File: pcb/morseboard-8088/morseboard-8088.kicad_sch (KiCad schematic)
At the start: 33 parts, among them J1 USB_B, SW1 SW_SPDT, SW3 RES, SW4 NMI, U1 8088, U2 74HCT573, U3 74HCT573, U4 74HCT245, U5 SST39SF040, U7 74HCT02, U8 74HCT00, U9 AS6C4008-55PCN, X1 TCXO-14

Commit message: Initial commit TL16C550
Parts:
- added U10: 74HCT273, Package_DIP:DIP-20_W7.62mm_Socket, symbol 74xx:74HC273
- added U11: ~, symbol tl16c550:TL16C550C-FN
- added U6: 74HCT138, Package_DIP:DIP-16_W7.62mm_Socket, symbol 74xx:74HC138
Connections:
- net A0: now also U11.31 (A0)
- net A1: now also U11.30 (A1)
- net A2: now also U11.29 (A2)
- net A5: now also U6.1 (A0)
- net A6: now also U6.2 (A1)
- net A7: now also U6.3 (A2)
- net D0: now also U10.3 (D0), U11.2 (D0)
- net D1: now also U10.4 (D1), U11.3 (D1)
- net D2: now also U10.7 (D2), U11.4 (D2)
- net D3: now also U10.8 (D3), U11.5 (D3)
- net D4: now also U10.13 (D4), U11.6 (D4)
- net D5: now also U10.14 (D5), U11.7 (D5)
- net D6: now also U10.17 (D6), U11.8 (D6)
- net D7: now also U10.18 (D7), U11.9 (D7)
- net GND: now also U10.10 (GND), U11.21 (WR2), U11.22 (GND), U11.25 (RD2), U11.28 (~{ADS}), U6.4 (~{E0}), U6.5 (~{E1}), U6.8 (GND); no longer U1.18 (INTR)
- net LATCH: now also U10.11 (Cp)
- net RES: now also U11.39 (MR)
- net VCC: now also U10.20 (VCC), U11.14 (CS0), U11.15 (CS1), U11.44 (VCC), U6.16 (VCC)
- net ~{IO00}: now also U6.15 (~{Y0})
- net ~{M}: now also U6.6 (E2)
- net ~{RD}: now also U11.24 (~{RD1})
- net ~{RES}: now also U10.1 (~{Mr})
- net ~{WR}: now also U11.20 (~{WR1})
- net ~{INTA}: now reaches U1.24 (~{INTA})
- new net INTR: U1.18 (INTR), U11.33 (INTRPT)
- new net L0: U10.2 (Q0)
- new net L1: U10.5 (Q1)
- new net L2: U10.6 (Q2)
- new net L3: U10.9 (Q3)
- new net L4: U10.12 (Q4)
- new net L5: U10.15 (Q5)
- new net L6: U10.16 (Q6)
- new net L7: U10.19 (Q7)
- new net RxD: U11.11 (SIN)
- new net TxD: U11.13 (SOUT)
- new net ~{IO01}: U11.16 (~{CS2}), U6.14 (~{Y1})
- no-connect marks 12 -> 20
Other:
- removed sheet output

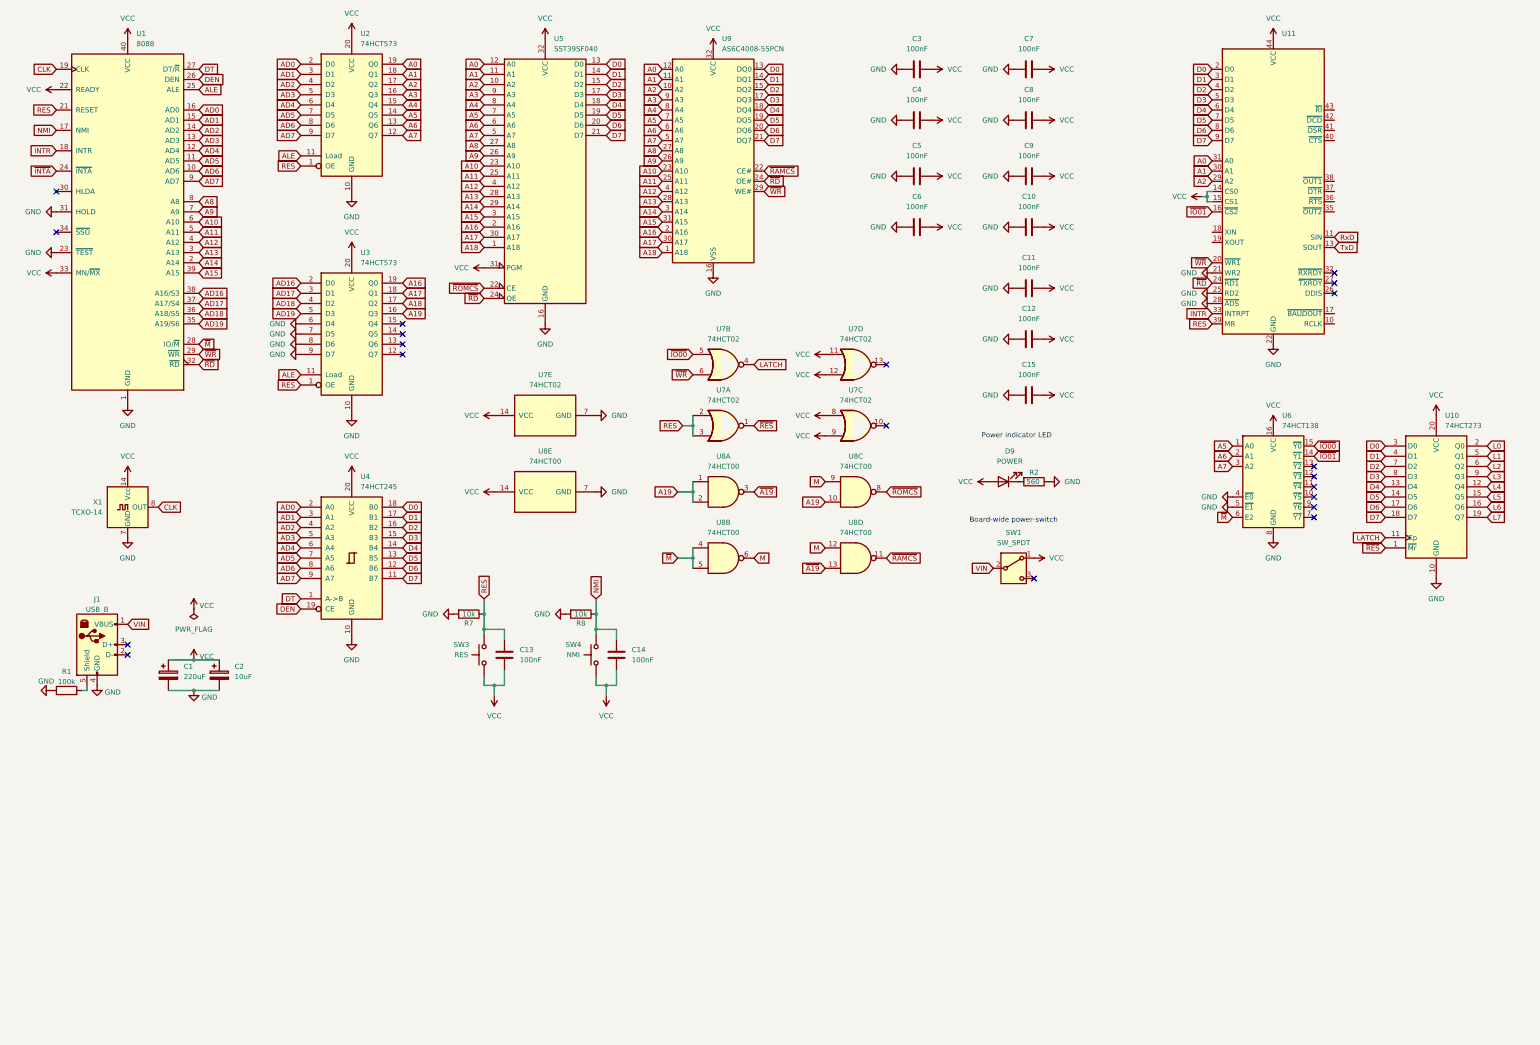
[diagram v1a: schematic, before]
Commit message: Further revising second 8088 SBC prototype
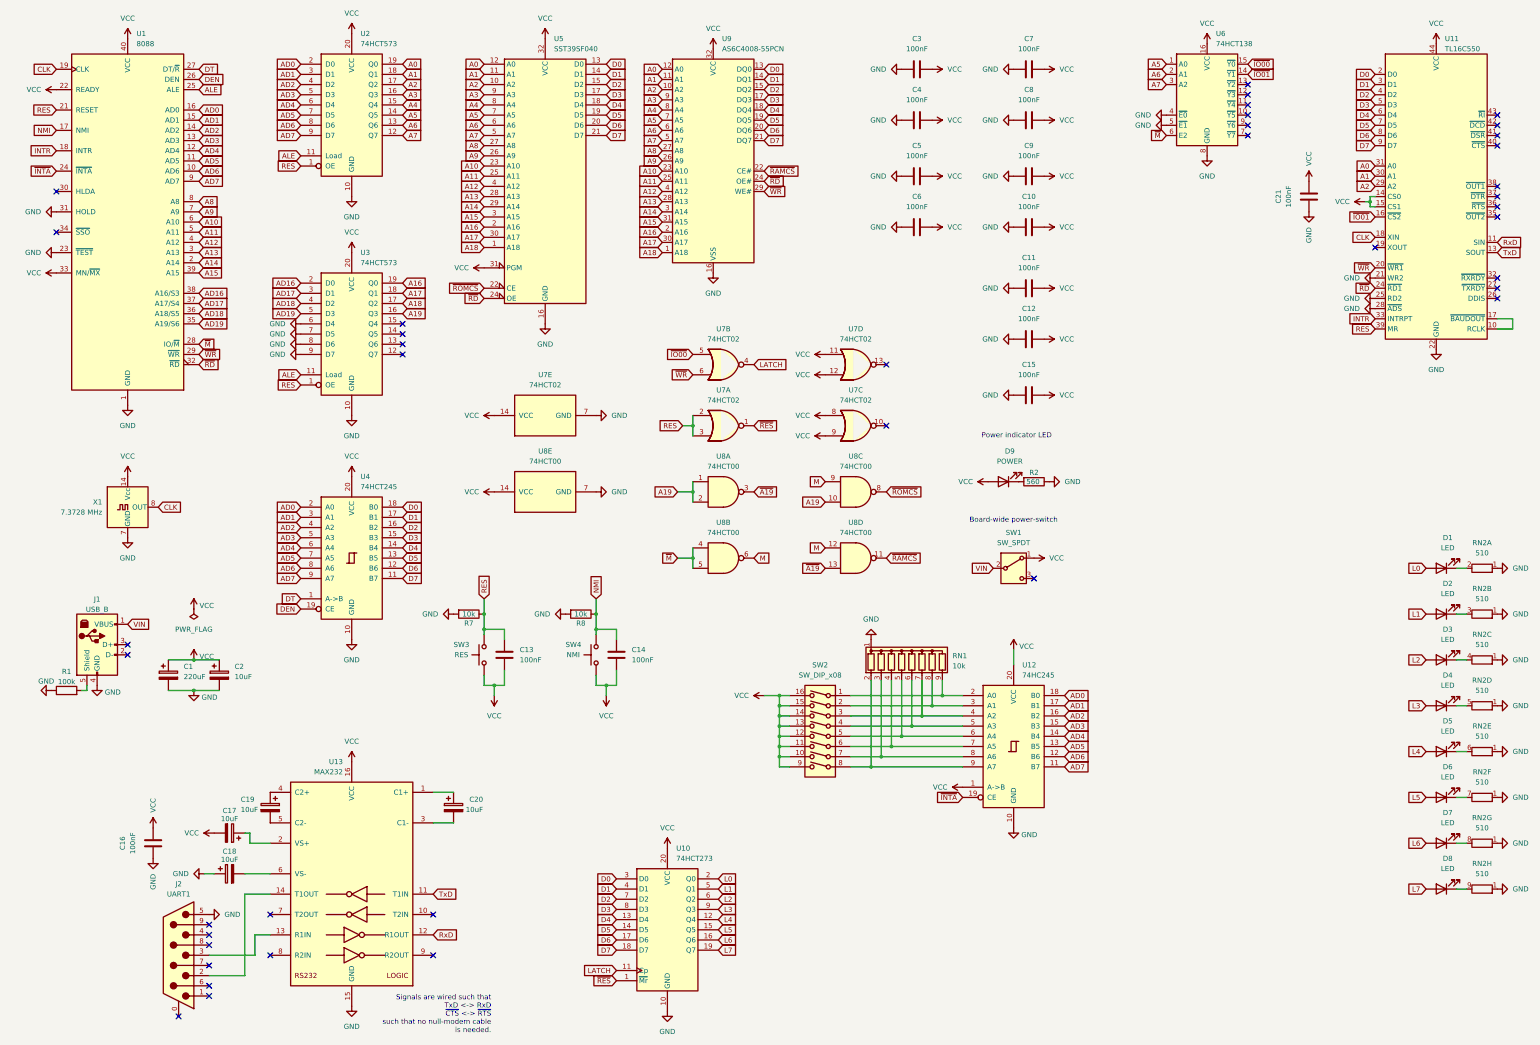
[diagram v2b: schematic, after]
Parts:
- added C16, C21: 100nF, Capacitor_THT:C_Disc_D5.0mm_W2.5mm_P5.00mm, symbol Device:C
- added C17, C18, C19, C20: 10uF, Capacitor_THT:CP_Radial_D5.0mm_P2.50mm, symbol Device:C_Polarized
- added D1, D2, D3, D4, D5, D6, D7, D8: LED, LED_THT:LED_D5.0mm, symbol Device:LED
- added J2: UART1, Connector_Dsub:DSUB-9_Pins_Horizontal_P2.77x2.84mm_EdgePinOffset4.94mm_Housed_MountingHolesOffset4.94mm, symbol Connector:DE9_Pins_MountingHoles
- added RN1: 10k, Resistor_THT:R_Array_SIP9, symbol Device:R_Network08
- added RN2: 510, Resistor_THT:R_Array_SIP9, symbol Device:R_Network08_Split
- added SW2: SW_DIP_x08, Button_Switch_THT:SW_DIP_SPSTx08_Slide_9.78x22.5mm_W7.62mm_P2.54mm, symbol Switch:SW_DIP_x08
- added U12: 74HC245, Package_DIP:DIP-20_W7.62mm_Socket, symbol 74xx:74HC245
- added U13: MAX232, Package_DIP:DIP-16_W7.62mm_Socket, symbol Interface_UART:MAX232
- U11: value ~ -> TL16C550; footprint (none) -> Package_LCC:PLCC-44_THT-Socket
- X1: value TCXO-14 -> 7.3728 MHz
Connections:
- net AD0: now also U12.18 (B0)
- net AD1: now also U12.17 (B1)
- net AD2: now also U12.16 (B2)
- net AD3: now also U12.15 (B3)
- net AD4: now also U12.14 (B4)
- net AD5: now also U12.13 (B5)
- net AD6: now also U12.12 (B6)
- net AD7: now also U12.11 (B7)
- net CLK: now also U11.18 (XIN)
- net GND: now also C16.2, C18.1, C21.2, J2.5, RN1.1 (common), RN2.1 (R1), RN2.1 (R1), RN2.1 (R1), RN2.1 (R1), RN2.1 (R1), RN2.1 (R1), RN2.1 (R1), RN2.1 (R1), U12.10 (GND), U13.15 (GND)
- net L0: now also D1.2 (A)
- net L1: now also D2.2 (A)
- net L2: now also D3.2 (A)
- net L3: now also D4.2 (A)
- net L4: now also D5.2 (A)
- net L5: now also D6.2 (A)
- net L6: now also D7.2 (A)
- net L7: now also D8.2 (A)
- net RxD: now also U13.12 (R1OUT)
- net TxD: now also U13.11 (T1IN)
- net VCC: now also C16.1, C17.2, C21.1, SW2.10, SW2.11, SW2.12, SW2.13, SW2.14, SW2.15, SW2.16, SW2.9, U12.1 (A->B), U12.20 (VCC), U13.16 (VCC)
- net ~{INTA}: now also U12.19 (CE)
- net at U11.10 (RCLK): now also U11.17 (~{BAUDOUT})
- new net: D5.1 (K), RN2.6 (R5.2)
- new net: D6.1 (K), RN2.7 (R6.2)
- new net: C17.1, U13.2 (VS+)
- new net: C18.2, U13.6 (VS-)
- new net: D3.1 (K), RN2.4 (R3.2)
- new net: D8.1 (K), RN2.9 (R8.2)
- new net: D2.1 (K), RN2.3 (R2.2)
- new net: J2.2, U13.14 (T1OUT)
- new net: J2.3, U13.13 (R1IN)
- new net: RN1.9 (R8), SW2.1, U12.2 (A0)
- new net: RN1.8 (R7), SW2.2, U12.3 (A1)
- new net: RN1.7 (R6), SW2.3, U12.4 (A2)
- new net: RN1.6 (R5), SW2.4, U12.5 (A3)
- new net: RN1.5 (R4), SW2.5, U12.6 (A4)
- new net: RN1.4 (R3), SW2.6, U12.7 (A5)
- new net: RN1.3 (R2), SW2.7, U12.8 (A6)
- new net: RN1.2 (R1), SW2.8, U12.9 (A7)
- new net: C20.1, U13.1 (C1+)
- new net: C20.2, U13.3 (C1-)
- new net: C19.1, U13.4 (C2+)
- new net: C19.2, U13.5 (C2-)
- new net: D1.1 (K), RN2.2 (R1.2)
- new net: D7.1 (K), RN2.8 (R7.2)
- new net: D4.1 (K), RN2.5 (R4.2)
- no-connect marks 20 -> 40
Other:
- note added: "Signals are wired such that TxD <-> RxD ~{CTS} <-> ~{RTS} such that no null-modem cable is needed."
- moved on the sheet: U10, U11, U6

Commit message: Updating schematic and board
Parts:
- added H1, H2, H3, H4: MountingHole, MountingHole:MountingHole_3.2mm_M3_DIN965, symbol Mechanical:MountingHole
- added J3: TxD, Connector_PinHeader_2.54mm:PinHeader_1x03_P2.54mm_Vertical, symbol Connector:Conn_01x03_Pin
- added J4: ~{CTS}, Connector_PinHeader_2.54mm:PinHeader_1x03_P2.54mm_Vertical, symbol Connector:Conn_01x03_Pin
- added J5: RxD, Connector_PinHeader_2.54mm:PinHeader_1x03_P2.54mm_Vertical, symbol Connector:Conn_01x03_Pin
- added J6: ~{RTS}, Connector_PinHeader_2.54mm:PinHeader_1x03_P2.54mm_Vertical, symbol Connector:Conn_01x03_Pin
- SW2: value SW_DIP_x08 -> INTPORT
- U1: footprint Package_DIP:DIP-40_W15.24mm -> Package_DIP:DIP-40_W15.24mm_Socket
- U9: footprint Package_DIP:DIP-32_W15.24mm -> Package_DIP:DIP-32_W15.24mm_Socket
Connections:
- net ~{RTS}: now reaches U11.36 (~{RTS})
- net ~{RTS}: now also U13.9 (R2OUT)
- net ~{CTS}: now reaches U11.40 (~{CTS})
- net ~{CTS}: now also U13.10 (T2IN)
- net T1OUT: now reaches U13.14 (T1OUT)
- net T1OUT: now also J3.2 (Pin_2); no longer J2.2
- net R1IN: now reaches U13.13 (R1IN)
- net R1IN: now also J5.2 (Pin_2); no longer J2.3
- net UART7: now reaches J2.7
- net UART7: now also J4.1 (Pin_1), J6.1 (Pin_1)
- net UART8: now reaches J2.8
- net UART8: now also J4.3 (Pin_3), J6.3 (Pin_3)
- net T2OUT: now reaches U13.7 (T2OUT)
- net T2OUT: now also J4.2 (Pin_2)
- net R2IN: now reaches U13.8 (R2IN)
- net R2IN: now also J6.2 (Pin_2)
- new net UART2: J2.2, J3.1 (Pin_1), J5.1 (Pin_1)
- new net UART3: J2.3, J3.3 (Pin_3), J5.3 (Pin_3)
- no-connect marks 40 -> 31
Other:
- moved on the sheet: C16, C17, C18, C19, C20, J2, U13

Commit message: Prerouting commit
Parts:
- removed C13: 100nF, Capacitor_THT:C_Disc_D5.0mm_W2.5mm_P5.00mm, symbol Device:C
- removed R7: 10k, Resistor_THT:R_Axial_DIN0207_L6.3mm_D2.5mm_P7.62mm_Horizontal, symbol Device:R
- removed SW3: RES, Button_Switch_THT:SW_PUSH_6mm, symbol Switch:SW_Push
- added SW6: RESET, Button_Switch_THT:SW_PUSH_6mm, symbol Switch:SW_Push
- added U14: DS1813, Package_TO_SOT_THT:TO-92, symbol Connector:Conn_01x03_Pin
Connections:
- net GND: now also SW6.1, U14.3 (Pin_3)
- net RES: now also U7.1; no longer U7.2, U7.3
- net VCC: now also U14.2 (Pin_2)
- net ~{CTS}: now also U13.9 (R2OUT); no longer U13.10 (T2IN)
- net ~{RES}: now also U7.2, U7.3, SW6.2, U14.1 (Pin_1); no longer U7.1
- net ~{RTS}: now also U13.10 (T2IN); no longer U13.9 (R2OUT)
- no-connect marks 31 -> 32
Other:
- note added: "0x00"
- note added: "0x20"

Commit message: Protoype #1 of SBC
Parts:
- added C13: 100nF, Capacitor_THT:C_Disc_D5.0mm_W2.5mm_P5.00mm, symbol Device:C
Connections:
- net GND: now also C13.2
- net VCC: now also C13.1
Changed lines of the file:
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@@
 	)
 	(symbol
+		(lib_id "power:VCC")
+		(at 299.72 113.03 270)
+		(unit 1)
+		(exclude_from_sim no)
+		(in_bom yes)
+		(on_board yes)
+		(dnp no)
+		(fields_autoplaced yes)
+		(property "Reference" "#PWR076"
+			(at 295.91 113.03 0)
+			(effects
+				(font
+					(size 1.27 1.27)
+				)
+				(hide yes)
+			)
+		)
+		(property "Value" "VCC"
+			(at 303.53 113.0299 90)
+			(effects
+				(font
+					(size 1.27 1.27)
+				)
+				(justify left)
+			)
+		)
+		(property "Footprint" ""
+			(at 299.72 113.03 0)
+			(effects
+				(font
+					(size 1.27 1.27)
+				)
+				(hide yes)
+			)
+		)
+		(property "Datasheet" ""
+			(at 299.72 113.03 0)
+			(effects
+				(font
+					(size 1.27 1.27)
+				)
+				(hide yes)
+			)
+		)
+		(property "Description" "Power symbol creates a global label with name \"VCC\""
+			(at 299.72 113.03 0)
+			(effects
+				(font
+					(size 1.27 1.27)
+				)
+				(hide yes)
+			)
+		)
+		(pin "1"
+		)
+		(instances
+			(project "morseboard-8088"
+				(path "/27cb38f9-12de-466e-a080-2dfa091752ed"
+					(reference "#PWR076")
+					(unit 1)
+				)
+			)
+		)
+	)
+	(symbol
 		(lib_id "power:GND")
 		(at 43.18 148.59 0)
@@
 	(symbol
 		(lib_id "power:GND")
+		(at 292.1 113.03 270)
+		(unit 1)
+		(exclude_from_sim no)
+		(in_bom yes)
+		(on_board yes)
+		(dnp no)
+		(fields_autoplaced yes)
+		(property "Reference" "#PWR075"
+			(at 285.75 113.03 0)
+			(effects
+				(font
+					(size 1.27 1.27)
+				)
+				(hide yes)
+			)
+		)
+		(property "Value" "GND"
+			(at 288.29 113.0299 90)
+			(effects
+				(font
+					(size 1.27 1.27)
+				)
+				(justify right)
+			)
+		)
+		(property "Footprint" ""
+			(at 292.1 113.03 0)
+			(effects
+				(font
+					(size 1.27 1.27)
+				)
+				(hide yes)
+			)
+		)
+		(property "Datasheet" ""
+			(at 292.1 113.03 0)
+			(effects
+				(font
+					(size 1.27 1.27)
+				)
+				(hide yes)
+			)
+		)
+		(property "Description" "Power symbol creates a global label with name \"GND\" , ground"
+			(at 292.1 113.03 0)
+			(effects
+				(font
+					(size 1.27 1.27)
+				)
+				(hide yes)
+			)
+		)
+		(pin "1"
+		)
+		(instances
+			(project "morseboard-8088"
+				(path "/27cb38f9-12de-466e-a080-2dfa091752ed"
+					(reference "#PWR075")
+					(unit 1)
+				)
+			)
+		)
+	)
+	(symbol
+		(lib_id "power:GND")
 		(at 99.06 118.11 0)
 		(unit 1)
@@
 					(unit 1)
 				)
+			)
+		)
+	)
+	(symbol
+		(lib_id "Device:C")
+		(at 295.91 113.03 270)
+		(unit 1)
+		(exclude_from_sim no)
+		(in_bom yes)
+		(on_board yes)
+		(dnp no)
+		(fields_autoplaced yes)
+		(property "Reference" "C13"
+			(at 295.91 105.41 90)
+			(effects
+				(font
+					(size 1.27 1.27)
+				)
+			)
+		)
+		(property "Value" "100nF"
+			(at 295.91 107.95 90)
+			(effects
+				(font
+					(size 1.27 1.27)
+				)
+			)
+		)
+		(property "Footprint" "Capacitor_THT:C_Disc_D5.0mm_W2.5mm_P5.00mm"
+			(at 292.1 113.9952 0)
+			(effects
+				(font
+					(size 1.27 1.27)
+				)
+				(hide yes)
+			)
+		)
+		(property "Datasheet" "~"
+			(at 295.91 113.03 0)
+			(effects
+				(font
+					(size 1.27 1.27)
+				)
+				(hide yes)
+			)
+		)
+		(property "Description" "Unpolarized capacitor"
+			(at 295.91 113.03 0)
+			(effects
+				(font
+					(size 1.27 1.27)
+				)
+				(hide yes)
+			)
+		)
+		(pin "1"
+		)
+		(pin "2"
+		)
+		(instances
+			(project "morseboard-8088"
+				(path "/27cb38f9-12de-466e-a080-2dfa091752ed"
+					(reference "C13")
+					(unit 1)
+				)

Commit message: Tuning UART
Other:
- note added: "08: ~{CTS} 03: TxD 07: ~{RTS} 02: RxD"
- note removed: "Signals are wired such that TxD <-> RxD ~{CTS} <-> ~{RTS} such that no null-modem cable is needed."
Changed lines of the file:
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@@
 		)
 	)
-	(text "Signals are wired such that\nTxD <-> RxD\n~{CTS} <-> ~{RTS}\nsuch that no null-modem cable\nis needed."
+	(text "08: ~{CTS}\n03: TxD\n07: ~{RTS}\n02: RxD"
 		(exclude_from_sim no)
-		(at 119.888 257.302 0)
+		(at 146.558 217.17 0)
 		(effects
 			(font
 				(size 1.27 1.27)
 			)
-			(justify right)
 		)
 	)

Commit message: Interim commit
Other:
- note added: "External hook-up: 08: ~{CTS} 03: TxD 07: ~{RTS} 02: RxD"
- note removed: "08: ~{CTS} 03: TxD 07: ~{RTS} 02: RxD"
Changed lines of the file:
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@@
 		)
 	)
-	(text "08: ~{CTS}\n03: TxD\n07: ~{RTS}\n02: RxD"
+	(text "External hook-up:\n08: ~{CTS}\n03: TxD\n07: ~{RTS}\n02: RxD"
 		(exclude_from_sim no)
-		(at 146.558 217.17 0)
+		(at 142.494 217.17 0)
 		(effects
 			(font
 				(size 1.27 1.27)
 			)
+			(justify left)
 		)
 	)
